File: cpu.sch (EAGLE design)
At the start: 13 parts

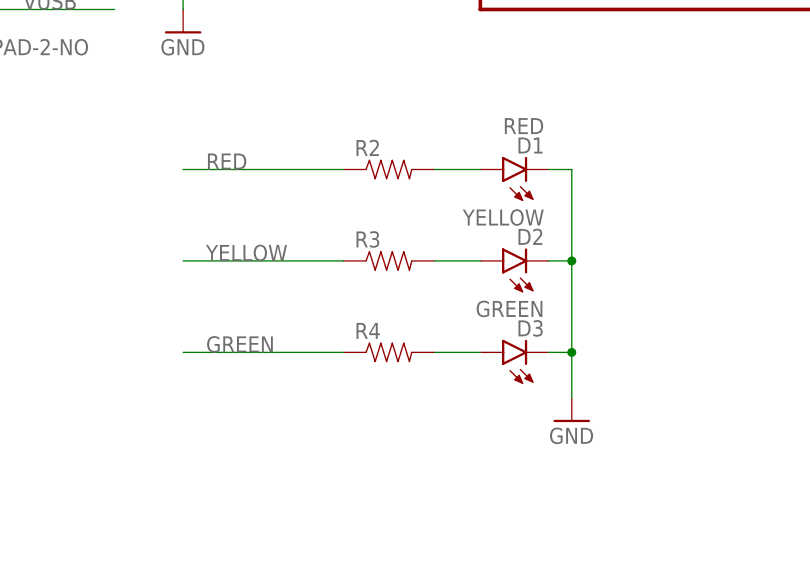
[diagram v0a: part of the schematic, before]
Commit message: Renamed bits on cpu
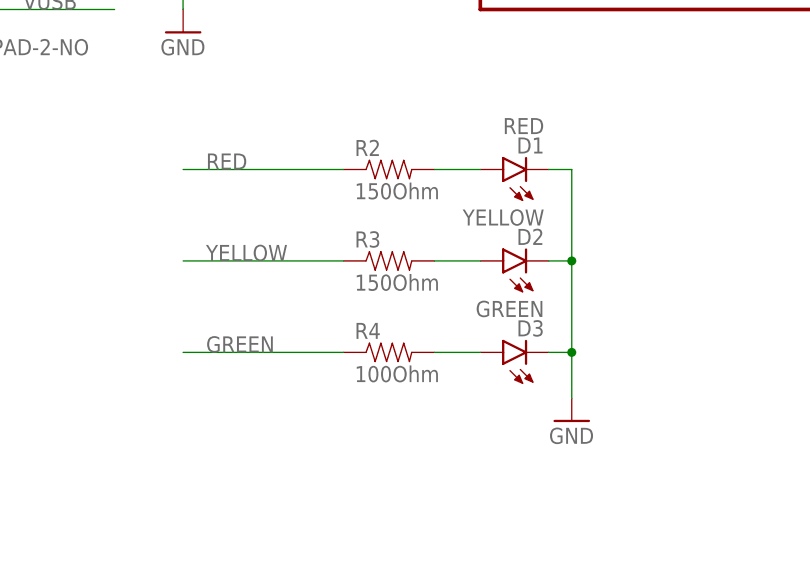
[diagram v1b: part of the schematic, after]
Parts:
- R2, R3: value (none) -> 150Ohm
- R4: value (none) -> 100Ohm
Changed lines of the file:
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@@
 <part name="D2" library="SparkFun-LED" deviceset="LED-YELLOW" device="0603" value="YELLOW"/>
 <part name="D3" library="SparkFun-LED" deviceset="LED-GREEN" device="0603" value="GREEN"/>
-<part name="R2" library="SparkFun-Passives" deviceset="RESISTOR" device="0402-RES"/>
-<part name="R3" library="SparkFun-Passives" deviceset="RESISTOR" device="0402-RES"/>
-<part name="R4" library="SparkFun-Passives" deviceset="RESISTOR" device="0402-RES"/>
+<part name="R2" library="SparkFun-Passives" deviceset="RESISTOR" device="0402-RES" value="150Ohm"/>
+<part name="R3" library="SparkFun-Passives" deviceset="RESISTOR" device="0402-RES" value="150Ohm"/>
+<part name="R4" library="SparkFun-Passives" deviceset="RESISTOR" device="0402-RES" value="100Ohm"/>
 <part name="GND2" library="supply1" deviceset="GND" device=""/>
 </parts>
